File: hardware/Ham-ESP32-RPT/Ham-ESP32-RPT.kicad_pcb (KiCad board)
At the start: 2 copper layers, 100 x 115 mm, 9 parts, among them J5 Conn_01x04_Socket, Q1 MMBT3904, SW1 REP TEST, U4 ESP32-S3-DevKitC

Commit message: PCB kicad update
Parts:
- removed SW1: REP TEST, Button_Switch_THT:SW_PUSH_6mm
- removed U4: ESP32-S3-DevKitC, PCM_Espressif:ESP32-S3-DevKitC
- added D3: GREEN, LED_SMD:LED_1206_3216Metric, F.Cu at (161.5, 54.9)
- added F1: 2A, Fuse:Fuse_1206_3216Metric, F.Cu at (160.5, 139.6)
- added F2: 4A, Fuse:Fuse_1206_3216Metric, F.Cu at (152.0, 141.1)
- added F3: 4A, Fuse:Fuse_1206_3216Metric, F.Cu at (132.5, 141.6)
- added FB2: VK200, Inductor_SMD:L_Neosid_MicroCoil_Ms36-L, F.Cu at (154.5, 122.5)
- added FB3: VK200, Inductor_SMD:L_Neosid_MicroCoil_Ms36-L, F.Cu at (137.5, 122.5)
- added FB4: VK200, Inductor_SMD:L_Neosid_MicroCoil_Ms36-L, F.Cu at (146.0, 122.5)
- added J1: 5V SUPPLY, Connector_JST:JST_XH_B2B-XH-A_1x02_P2.50mm_Vertical, F.Cu at (162.5, 148.0)
- added J2: 12V SUPPLY, Connector_JST:JST_XH_B2B-XH-A_1x02_P2.50mm_Vertical, F.Cu at (97.5, 148.0)
- added J3: RX RADIO, Connector_JST:JST_XH_B5B-XH-A_1x05_P2.50mm_Vertical, F.Cu at (142.0, 148.0)
- added J4: TX RADIO, Connector_JST:JST_XH_B4B-XH-A_1x04_P2.50mm_Vertical, F.Cu at (125.0, 148.0)
- added J6: SPEAKER, Connector_JST:JST_XH_B2B-XH-A_1x02_P2.50mm_Vertical, F.Cu at (77.5, 98.0)
- added R3: 330R, Resistor_SMD:R_1206_3216Metric, F.Cu at (168.0, 49.0)
- added R4: 330R, Resistor_SMD:R_1206_3216Metric, F.Cu at (161.5, 49.0)
- added SW2: TEST, Button_Switch_SMD:SW_Push_1P1T_NO_E-Switch_TL3301NxxxxxG, F.Cu at (146.0, 94.0)
- added U1: ESP32-S3-DevKitC-V2, Ham-ESP32-RPT-pretty:ESP32-S3-DevKitC-V2, F.Cu at (100.0, 69.4)
- added U3: INA219AxD, Package_SO:SOIC-8_3.9x4.9mm_P1.27mm, F.Cu at (131.0, 93.9)
- added VR1: 10K, Potentiometer_SMD:Potentiometer_Bourns_3314R-1_Vertical_Hole, F.Cu at (112.5, 122.5)
- added VR2: 10K, Potentiometer_SMD:Potentiometer_Bourns_3314R-1_Vertical_Hole, F.Cu at (129.0, 123.2)
- added VR3: 10K, Potentiometer_SMD:Potentiometer_Bourns_3314R-1_Vertical_Hole, F.Cu at (120.5, 123.0)
- D1: value GREEN -> BLUE
- FB1: value FerriteBead -> VK200; footprint Ferrite_THT:LairdTech_28C0236-0JW-10 -> Inductor_SMD:L_Neosid_MicroCoil_Ms36-L
- J5: value Conn_01x04_Socket -> AUX BTN LED; footprint Connector_JST:JST_XH_B4B-XH-A_1x04_P2.50mm_Vertical -> Connector_JST:JST_XH_B5B-XH-A_1x05_P2.50mm_Vertical
- Q1: value MMBT3904 -> MMBT2222A; footprint Package_TO_SOT_SMD:SOT-23 -> Package_TO_SOT_SMD:TSOT-23
- R2: value 330R -> 3.3K
- moved J5 109.4 mm to (76.5, 44.0), turned to 0 degrees
- moved FB1 96.4 mm to (163.5, 122.0), turned to 90 degrees
- moved D2 88.1 mm to (168.0, 54.6), turned to 90 degrees
- moved D1 83.6 mm to (163.6, 133.5), turned to 180 degrees
- moved R1 78.4 mm to (167.0, 139.5), turned to -90 degrees
- moved Q1 26.8 mm to (98.0, 84.5), turned to -90 degrees
- moved R2 15.5 mm to (105.0, 82.0), turned to 180 degrees
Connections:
- D1 pad 1: GND -> Net-(D1-K)
- FB1 pad 1: unconnected-(FB1-Pad1) -> Net-(D1-A)
- FB1 pad 2: unconnected-(FB1-Pad2) -> +5V
- Q1 pad 1: unconnected-(Q1-B-Pad1) -> Net-(Q1-B)
- Q1 pad 2: unconnected-(Q1-E-Pad2) -> GND
- Q1 pad 3: unconnected-(Q1-C-Pad3) -> Net-(J4-Pin_1)
- R1 pad 1: Net-(U4-GPIO9/ADC1_CH8) -> Net-(D1-K)
- R1 pad 2: Net-(D1-A) -> GND
- R2 pad 2: Net-(D2-A) -> Net-(Q1-B)

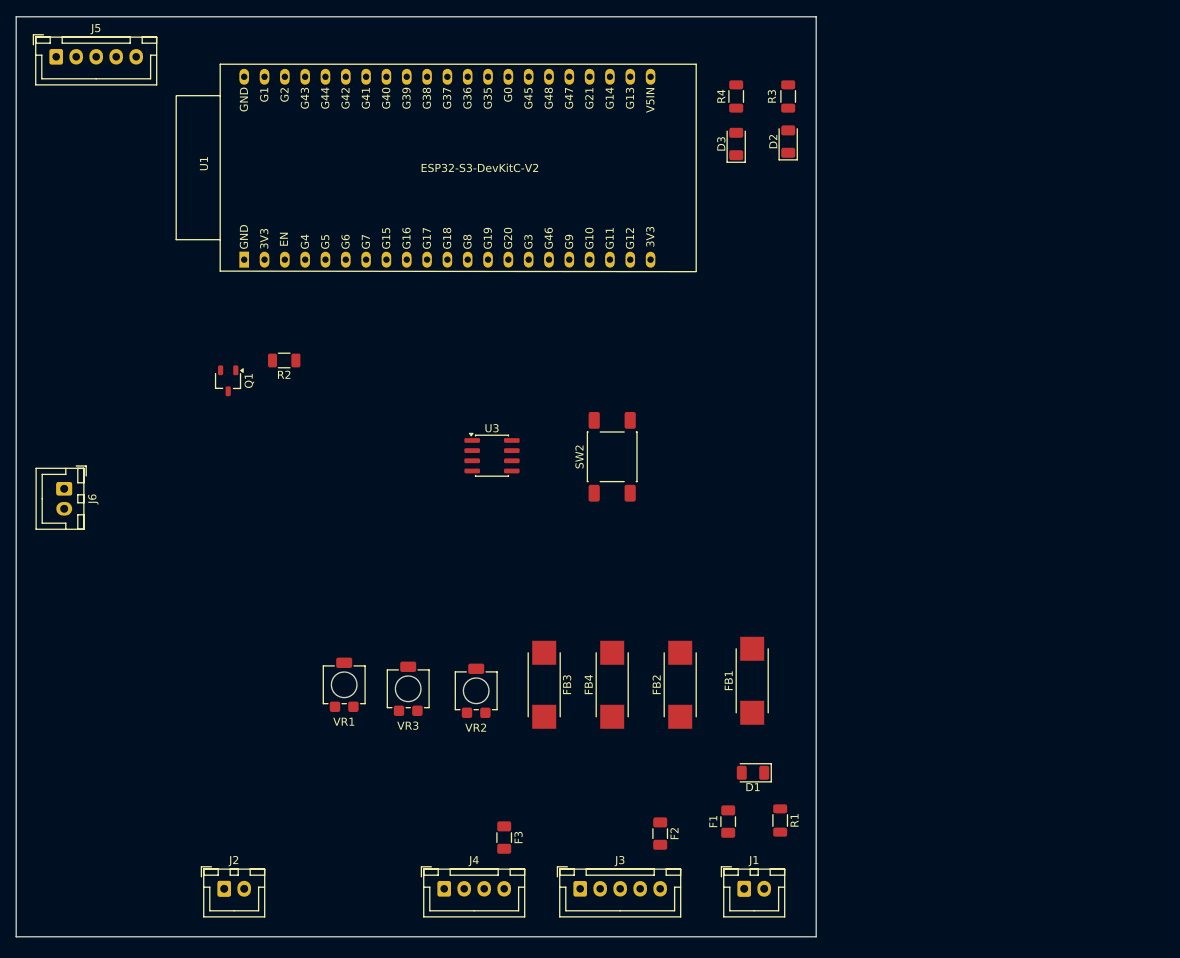
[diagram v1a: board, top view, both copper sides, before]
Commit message: Add Vk200 footprint
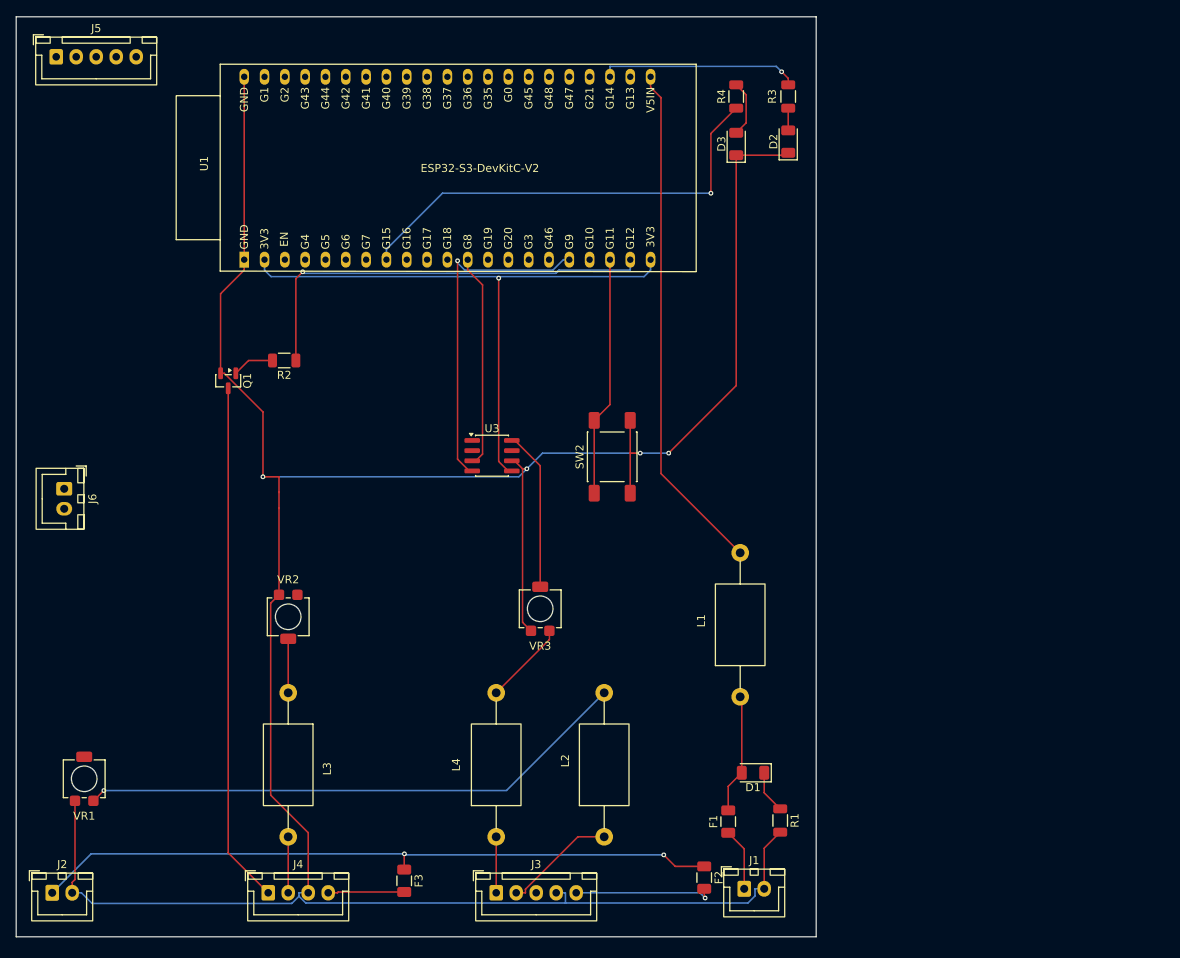
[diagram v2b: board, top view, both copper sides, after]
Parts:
- removed FB1, FB2, FB3, FB4: VK200, Inductor_SMD:L_Neosid_MicroCoil_Ms36-L
- added L1: VK200, Ham-ESP32-RPT-pretty:VK200, F.Cu at (162.0, 124.0)
- added L2: VK200, Ham-ESP32-RPT-pretty:VK200, F.Cu at (145.0, 141.5)
- added L3: VK200, Ham-ESP32-RPT-pretty:VK200, F.Cu at (105.5, 123.5)
- added L4: VK200, Ham-ESP32-RPT-pretty:VK200, F.Cu at (131.5, 141.5)
- Q1: footprint Package_TO_SOT_SMD:TSOT-23 -> Package_TO_SOT_SMD:SOT-23
- moved VR1 34.6 mm to (80.0, 134.2)
- moved VR2 25.3 mm to (105.5, 114.0), turned to 0 degrees
- moved J4 22.0 mm to (103.0, 148.5)
- moved J2 21.5 mm to (76.0, 148.5)
- moved VR3 19.3 mm to (137.0, 113.0)
- moved F3 13.6 mm to (120.0, 147.0)
- moved J3 10.5 mm to (131.5, 148.5)
- moved F2 7.78 mm to (157.5, 146.6)
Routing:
- net GND: track 0.00 -> 355.3 mm, vias 0 -> 4
- net Net-(J2-Pin_1): track 0.00 -> 86.2 mm, vias 0 -> 2
- net +3.3V: track 0.00 -> 76.8 mm, vias 0 -> 1
- net Net-(L2-Pad2): track 0.00 -> 69.4 mm, vias 0 -> 1
- net Net-(J4-Pin_1): track 0.00 -> 65.1 mm
- net +5V: track 0.00 -> 64.1 mm
- net Net-(U1-G15): track 0.00 -> 56.7 mm, vias 0 -> 1
- net Net-(U1-G12): track 0.00 -> 54.2 mm, vias 0 -> 1
- net Net-(U1-G9): track 0.00 -> 42.4 mm, vias 0 -> 1
- net Net-(U1-G11): track 0.00 -> 30.0 mm
- net Net-(U1-G8): track 0.00 -> 26.7 mm
- net Net-(U1-G14): track 0.00 -> 25.0 mm, vias 0 -> 1
- net Net-(U3-IN+): track 0.00 -> 20.0 mm
- net Net-(J3-Pin_5): track 0.00 -> 17.6 mm, vias 0 -> 1
- net Net-(D1-A): track 0.00 -> 15.0 mm
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
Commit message: Add PmodI2S2 footprint
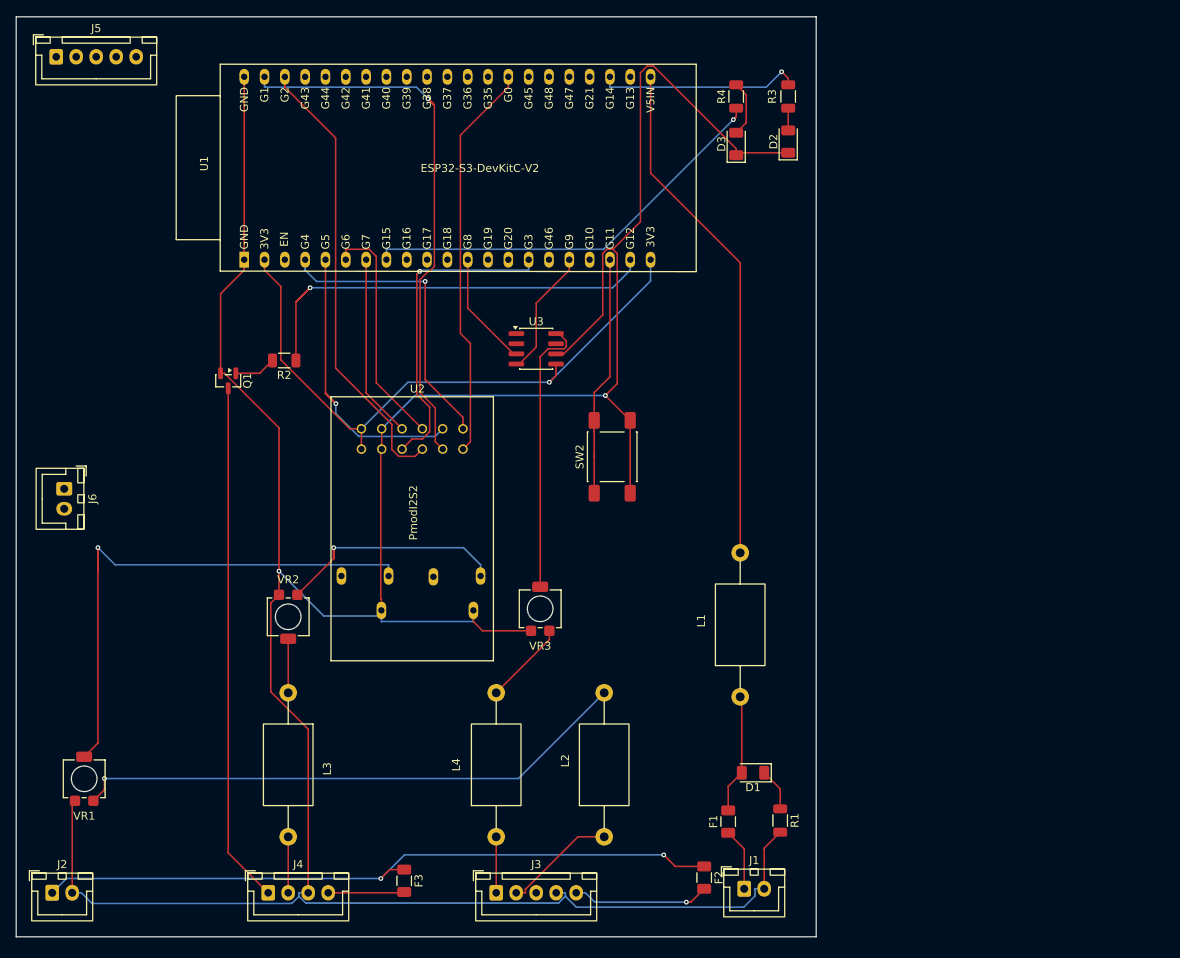
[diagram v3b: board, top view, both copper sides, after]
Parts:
- added U2: PmodI2S2, Ham-ESP32-RPT-pretty:PmodI2S2, F.Cu at (114.7, 90.5)
- moved U3 14.5 mm to (136.5, 80.5)
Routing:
- net Net-(U2-A_IN_L): track 0.00 -> 77.6 mm, vias 0 -> 1
- net Net-(U1-G1): track 0.00 -> 72.9 mm, vias 0 -> 1
- net Net-(U1-G2): track 0.00 -> 56.7 mm
- net GND: track 355.3 -> 409.9 mm, vias 4 -> 2
- net Net-(U1-G0): track 0.00 -> 49.9 mm
- net Net-(U1-G5): track 0.00 -> 42.1 mm, vias 0 -> 1
- net Net-(U1-G3): track 0.00 -> 40.6 mm, vias 0 -> 1
- net Net-(U1-G4): track 0.00 -> 37.5 mm, vias 0 -> 1
- net Net-(U2-A_OUT_L): track 0.00 -> 33.8 mm, vias 0 -> 1
- net Net-(U1-G6): track 0.00 -> 29.4 mm
- net Net-(U1-G9): track 42.4 -> 16.0 mm, vias 1 -> 0
- net Net-(U1-G7): track 0.00 -> 23.0 mm
- net Net-(U3-IN+): track 20.0 -> 34.9 mm
- net Net-(U1-G8): track 26.7 -> 14.5 mm
- net Net-(U1-G12): track 54.2 -> 62.1 mm
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
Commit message: Supression pistes
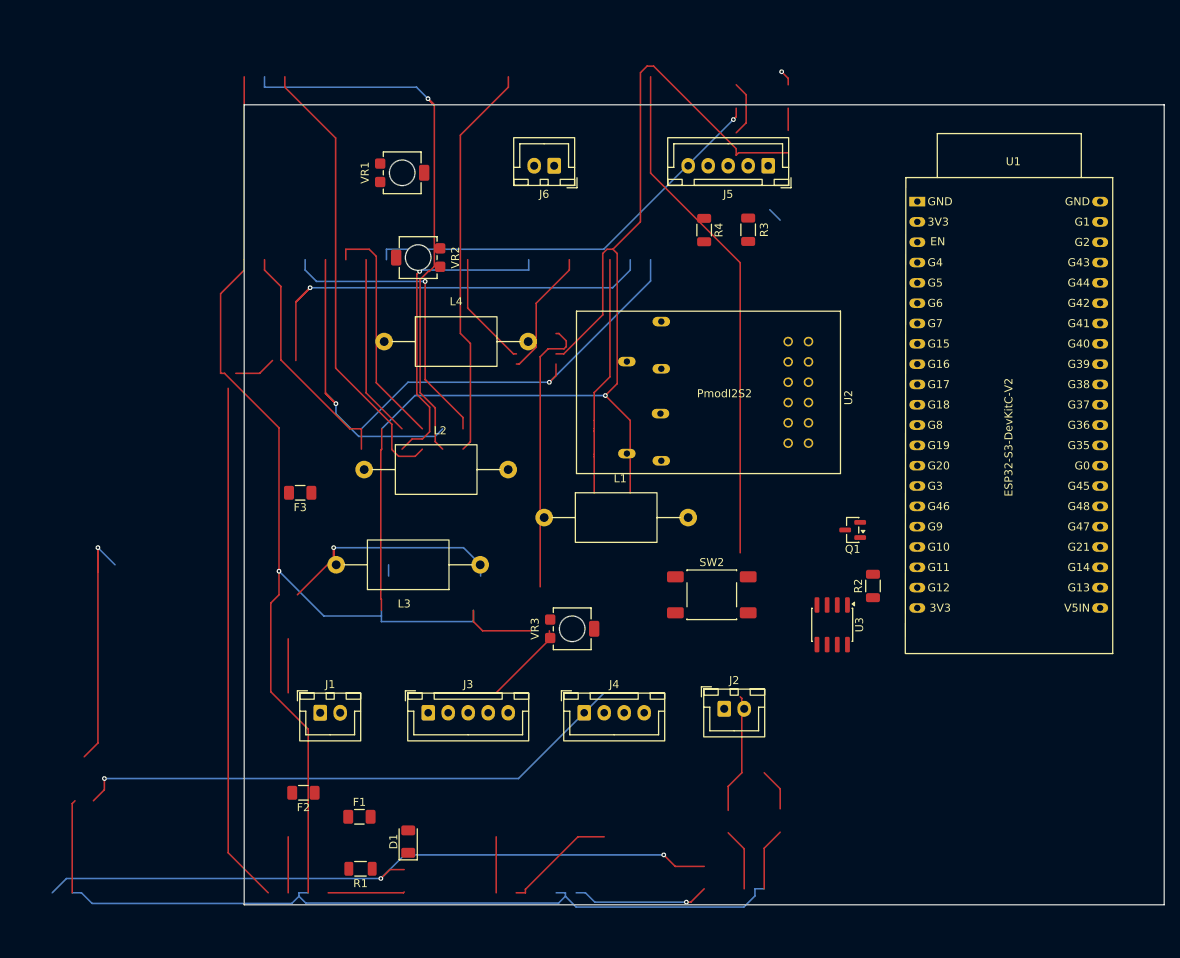
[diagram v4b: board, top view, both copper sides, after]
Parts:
- removed D2: RED, LED_SMD:LED_1206_3216Metric
- removed D3: GREEN, LED_SMD:LED_1206_3216Metric
- moved J5 90.0 mm to (165.5, 57.6), turned to 180 degrees
- moved J2 87.1 mm to (160.0, 125.5)
- moved VR1 85.5 mm to (119.8, 58.5), turned to 90 degrees
- moved U1 84.4 mm to (184.1, 62.1), turned to 0 degrees
- moved Q1 80.3 mm to (176.1, 103.1), turned to 180 degrees
- moved R2 78.8 mm to (178.6, 110.1), turned to 90 degrees
- moved J6 73.4 mm to (138.7, 57.6), turned to 180 degrees
- moved L4 63.5 mm to (117.5, 79.6), turned to 0 degrees
- moved J1 57.4 mm to (109.5, 126.0)
- moved U2 56.9 mm to (170.5, 79.6), turned to -90 degrees
- moved L2 54.8 mm to (115.0, 95.6), turned to 0 degrees
- moved R1 52.8 mm to (114.5, 145.5), turned to 180 degrees
- moved F2 51.2 mm to (107.4, 136.0), turned to 180 degrees
- moved U3 50.6 mm to (173.5, 115.0), turned to -90 degrees
- moved F3 50.2 mm to (107.0, 98.5), turned to 180 degrees
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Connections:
- J5 pad 1: unconnected-(J5-Pin_1-Pad1) -> GND
- J5 pad 2: unconnected-(J5-Pin_2-Pad2) -> Net-(J5-Pin_2)
- J5 pad 3: unconnected-(J5-Pin_3-Pad3) -> Net-(J5-Pin_3)
- J5 pad 4: unconnected-(J5-Pin_4-Pad4) -> Net-(J5-Pin_4)
- R3 pad 2: Net-(D2-A) -> Net-(J5-Pin_3)
- R4 pad 2: Net-(D3-A) -> Net-(J5-Pin_2)
- SW2 pad 1: Net-(U1-G11) -> Net-(J5-Pin_4)
- U1 pad 19: Net-(U1-G11) -> Net-(J5-Pin_4)
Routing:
- net Net-(U2-A_IN_L): track 77.6 -> 0.00 mm, vias 1 -> 0
- net Net-(U1-G1): track 72.9 -> 0.00 mm, vias 1 -> 0
- net GND: track 409.9 -> 481.5 mm
- net Net-(L2-Pad2): track 70.3 -> 0.00 mm, vias 1 -> 0
- net Net-(D1-A): track 15.0 -> 84.8 mm
- net Net-(J4-Pin_2): track 7.00 -> 72.9 mm, vias 0 -> 1
- net Net-(J2-Pin_1): track 87.4 -> 152.6 mm
- net Net-(U1-G2): track 56.7 -> 0.00 mm
- net Net-(L4-Pad2): track 10.5 -> 67.1 mm, vias 0 -> 1
- net unconnected-(J5-Pin_5-Pad5): track 0.00 -> 53.0 mm, vias 0 -> 1
- net Net-(U1-G0): track 49.9 -> 0.00 mm
- net unconnected-(J3-Pin_3-Pad3): track 0.00 -> 43.4 mm, vias 0 -> 1
- net Net-(U1-G3): track 40.6 -> 0.00 mm, vias 1 -> 0
- net Net-(U1-G4): track 37.5 -> 0.00 mm, vias 1 -> 0
- net Net-(U3-IN+): track 34.9 -> 0.00 mm
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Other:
- board size 100 x 115 mm -> 115 x 100 mm

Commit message: PCB Update
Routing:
- net GND: track 481.5 -> 351.4 mm, vias 2 -> 3
- net Net-(J5-Pin_4): track 0.00 -> 82.8 mm, vias 0 -> 1
- net Net-(U1-G14): track 0.00 -> 81.2 mm, vias 0 -> 1
- net Net-(U1-G1): track 0.00 -> 66.7 mm, vias 0 -> 1
- net Net-(U1-G2): track 0.00 -> 58.5 mm, vias 0 -> 1
- net Net-(J4-Pin_4): track 9.54 -> 65.9 mm, vias 0 -> 1
- net Net-(U1-G12): track 62.1 -> 6.06 mm, vias 1 -> 0
- net unconnected-(J5-Pin_5-Pad5): track 53.0 -> 0.00 mm, vias 1 -> 0
- net Net-(U2-A_OUT_L): track 0.00 -> 52.5 mm, vias 0 -> 1
- net Net-(U2-A_IN_L): track 0.00 -> 50.2 mm, vias 0 -> 1
- net Net-(J2-Pin_1): track 152.6 -> 103.0 mm
- net Net-(L2-Pad2): track 0.00 -> 48.2 mm, vias 0 -> 1
- net unconnected-(J3-Pin_3-Pad3): track 43.4 -> 0.00 mm, vias 1 -> 0
- net Net-(U1-G0): track 0.00 -> 43.0 mm
- net Net-(L3-Pad1): track 6.75 -> 44.7 mm, vias 0 -> 1
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- added copper zone on B.Cu, net GND

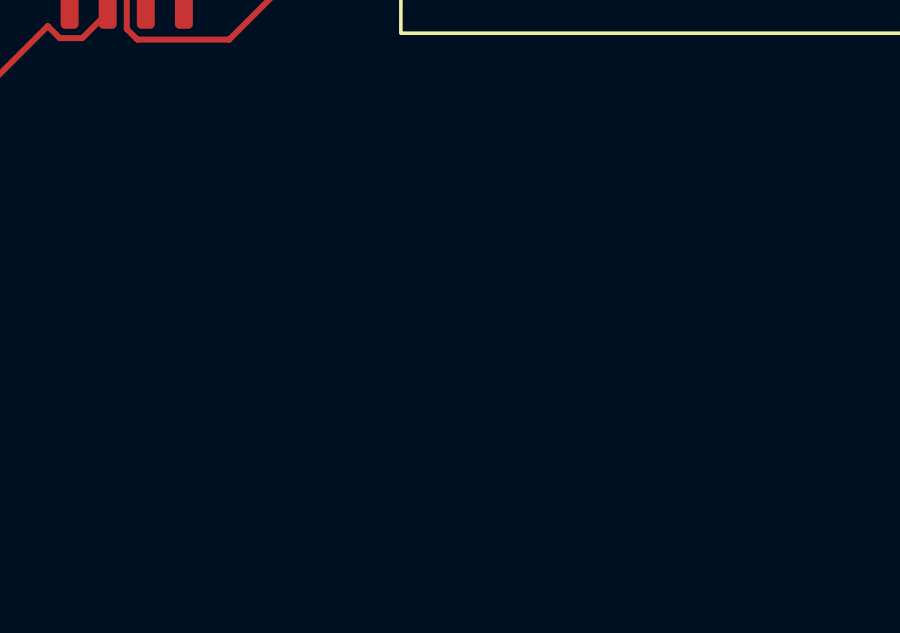
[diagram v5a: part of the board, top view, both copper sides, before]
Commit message: update PCB diagram
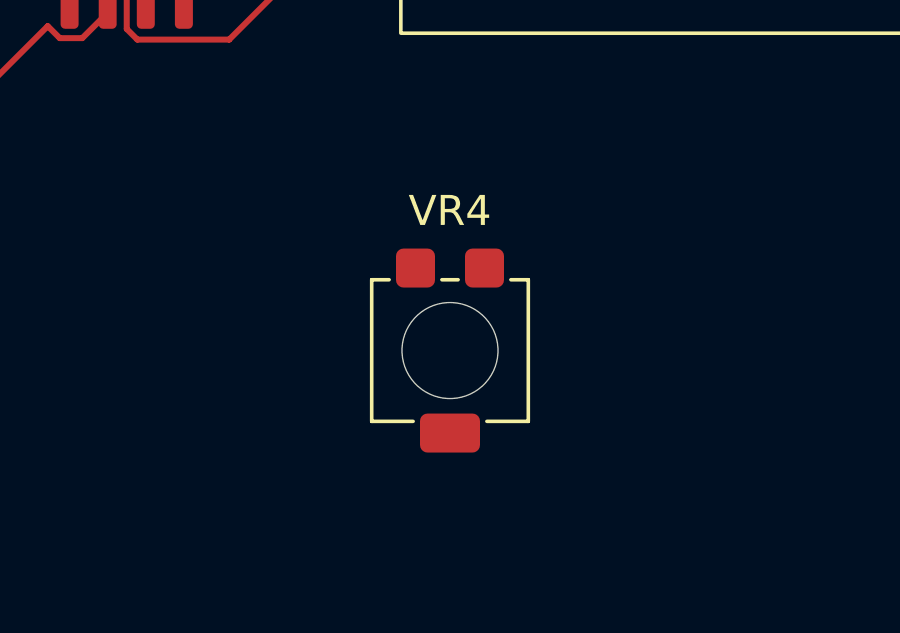
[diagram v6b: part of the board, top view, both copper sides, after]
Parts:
- added VR4: 10K, Potentiometer_SMD:Potentiometer_Bourns_3314R-1_Vertical_Hole, F.Cu at (184.3, 129.2)
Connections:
- J6 pad 1: unconnected-(J6-Pin_1-Pad1) -> Net-(J6-Pin_1)
- J6 pad 2: unconnected-(J6-Pin_2-Pad2) -> Net-(J6-Pin_2)
- VR3 pad 2: Net-(U3-IN+) -> Net-(U3-VIN-)
